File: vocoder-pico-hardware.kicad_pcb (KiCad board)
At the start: 2 copper layers, 47 x 108 mm, 68 parts, among them J1 Conn_02x05_Odd_Even, J2 AudioJack2_SwitchT, J3 AudioJack2_SwitchT, Q1 BC547, Q2 BC547, Q3 BC547, Q4 BC547, SW1 SW_Push, SW2 SW_Push, U1 TL072, U2 LM7805_TO220, U3 PCM5100A, U4 SC39-11GWA, U5 SC39-11GWA, U6 SC39-11GWA, U7 SC39-11GWA, U8 MCP6002-xP

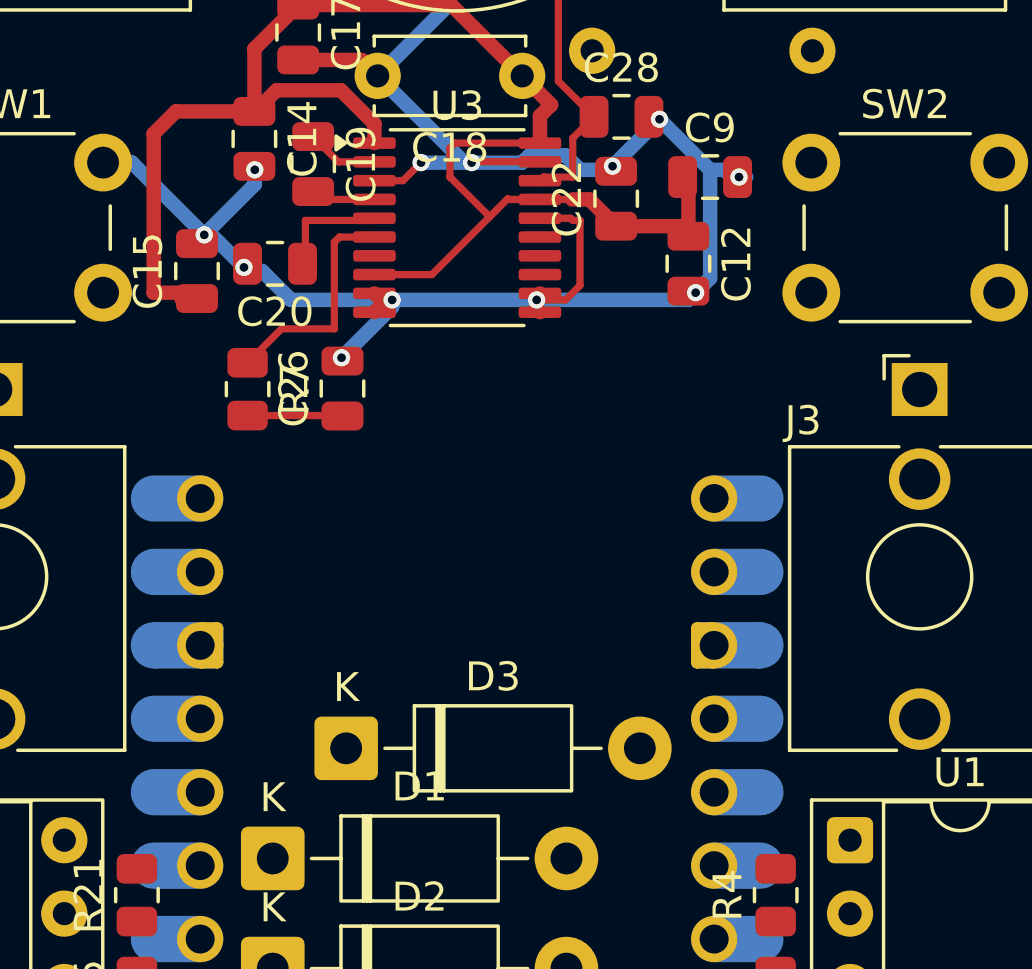
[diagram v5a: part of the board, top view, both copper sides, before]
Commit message: begin routing of i2s section
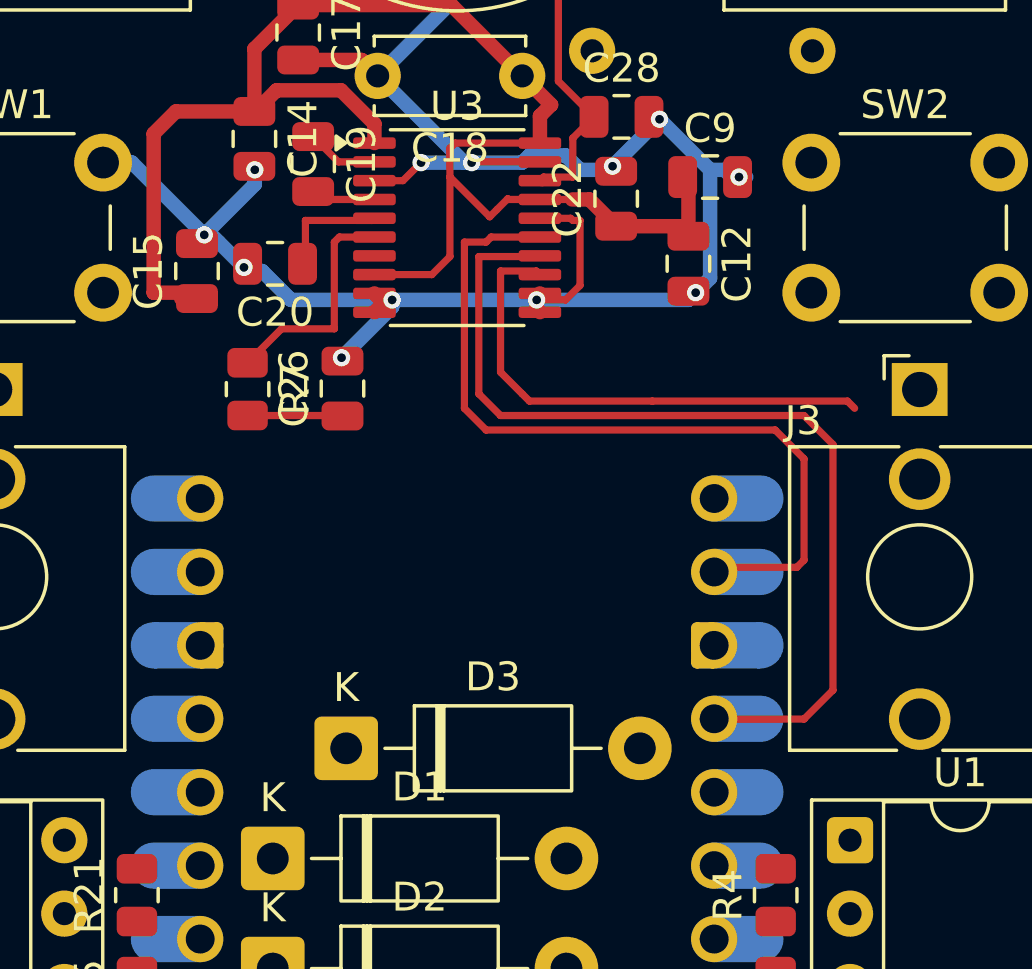
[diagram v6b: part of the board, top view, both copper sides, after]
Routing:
- net Net-(A1-GPIO18): track 0.00 -> 32.9 mm
- net Net-(A1-GPIO17): track 0.00 -> 27.7 mm
- net Net-(A1-GPIO16): track 0.00 -> 17.7 mm
- net Vdd: track 54.3 -> 55.1 mm
- net Net-(A1-GPIO12): track 0.00 -> 0.80 mm
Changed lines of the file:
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@@
+	)
+	(segment
+		(start 84.25 84)
+		(end 91 84)
+		(width 0.25)
+		(layer "F.Cu")
+		(net 9)
+	)
+	(segment
+		(start 79 83)
+		(end 79.75 83.75)
+		(width 0.25)
+		(layer "F.Cu")
+		(net 9)
+	)
+	(segment
+		(start 80.2375 79.5)
+		(end 79 79.5)
+		(width 0.25)
+		(layer "F.Cu")
+		(net 9)
+	)
+	(segment
+		(start 80 84)
+		(end 84.25 84)
+		(width 0.25)
+		(layer "F.Cu")
+		(net 9)
+	)
+	(segment
+		(start 79.75 83.75)
+		(end 80 84)
+		(width 0.25)
+		(layer "F.Cu")
+		(net 9)
+	)
+	(segment
+		(start 91 84)
+		(end 91.25 84.25)
+		(width 0.25)
+		(layer "F.Cu")
+		(net 9)
+	)
+	(segment
+		(start 80.3625 79.625)
+		(end 80.2375 79.5)
+		(width 0.25)
+		(layer "F.Cu")
+		(net 9)
+	)
+	(segment
+		(start 79 79.5)
+		(end 79 83)
+		(width 0.25)
+		(layer "F.Cu")
+		(net 9)
 	)
 	(segment
@@
 	)
 	(segment
+		(start 77.25 79)
+		(end 77.25 76.25)
+		(width 0.25)
+		(layer "F.Cu")
+		(net 20)
+	)
+	(segment
 		(start 77.425 75.075)
 		(end 77.25 75.25)
@@
 	(segment
 		(start 76.625 79.625)
-		(end 78.625 77.625)
+		(end 77.25 79)
 		(width 0.25)
 		(layer "F.Cu")
@@
 	)
 	(segment
+		(start 86.55 89.75)
+		(end 86.39 89.91)
+		(width 0.25)
+		(layer "F.Cu")
+		(net 25)
+	)
+	(segment
+		(start 80.3625 78.325)
+		(end 78.675 78.325)
+		(width 0.25)
+		(layer "F.Cu")
+		(net 25)
+	)
+	(segment
+		(start 89.5 89.5)
+		(end 89.25 89.75)
+		(width 0.25)
+		(layer "F.Cu")
+		(net 25)
+	)
+	(segment
+		(start 78.675 78.325)
+		(end 78.5 78.5)
+		(width 0.25)
+		(layer "F.Cu")
+		(net 25)
+	)
+	(segment
+		(start 89.5 86)
+		(end 89.5 89.5)
+		(width 0.25)
+		(layer "F.Cu")
+		(net 25)
+	)
+	(segment
+		(start 88.5 85)
+		(end 89.5 86)
+		(width 0.25)
+		(layer "F.Cu")
+		(net 25)
+	)
+	(segment
+		(start 77.75 78.5)
+		(end 77.75 84.25)
+		(width 0.25)
+		(layer "F.Cu")
+		(net 25)
+	)
+	(segment
+		(start 89.25 89.75)
+		(end 86.55 89.75)
+		(width 0.25)
+		(layer "F.Cu")
+		(net 25)
+	)
+	(segment
+		(start 77.75 84.25)
+		(end 78.5 85)
+		(width 0.25)
+		(layer "F.Cu")
+		(net 25)
+	)
+	(segment
+		(start 78.5 78.5)
+		(end 77.75 78.5)
+		(width 0.25)
+		(layer "F.Cu")
+		(net 25)
+	)
+	(segment
+		(start 78.5 85)
+		(end 88.5 85)
+		(width 0.25)
+		(layer "F.Cu")
+		(net 25)
+	)
+	(segment
+		(start 79 84.5)
+		(end 89.5 84.5)
+		(width 0.25)
+		(layer "F.Cu")
+		(net 28)
+	)
+	(segment
+		(start 86.4 95)
+		(end 86.39 94.99)
+		(width 0.25)
+		(layer "F.Cu")
+		(net 28)
+	)
+	(segment
+		(start 78.25 83.75)
+		(end 79 84.5)
+		(width 0.25)
+		(layer "F.Cu")
+		(net 28)
+	)
+	(segment
+		(start 90.5 94)
+		(end 89.5 95)
+		(width 0.25)
+		(layer "F.Cu")
+		(net 28)
+	)
+	(segment
+		(start 78.25 79)
+		(end 78.25 83.75)
+		(width 0.25)
+		(layer "F.Cu")
+		(net 28)
+	)
+	(segment
+		(start 80.3375 79)
+		(end 78.25 79)
+		(width 0.25)
+		(layer "F.Cu")
+		(net 28)
+	)
+	(segment
+		(start 80.3625 78.975)
+		(end 80.3375 79)
+		(width 0.25)
+		(layer "F.Cu")
+		(net 28)
+	)
+	(segment
+		(start 90.5 85.5)
+		(end 90.5 94)
+		(width 0.25)
+		(layer "F.Cu")
+		(net 28)
+	)
+	(segment
+		(start 89.5 84.5)
+		(end 90.5 85.5)
+		(width 0.25)
+		(layer "F.Cu")
+		(net 28)
+	)
+	(segment
+		(start 89.5 95)
+		(end 86.4 95)
+		(width 0.25)
+		(layer "F.Cu")
+		(net 28)
+	)
+	(segment
+		(start 67.81 97.53)
+		(end 68.61 97.53)
+		(width 0.25)
+		(layer "B.Cu")
+		(net 34)
+	)
+	(segment

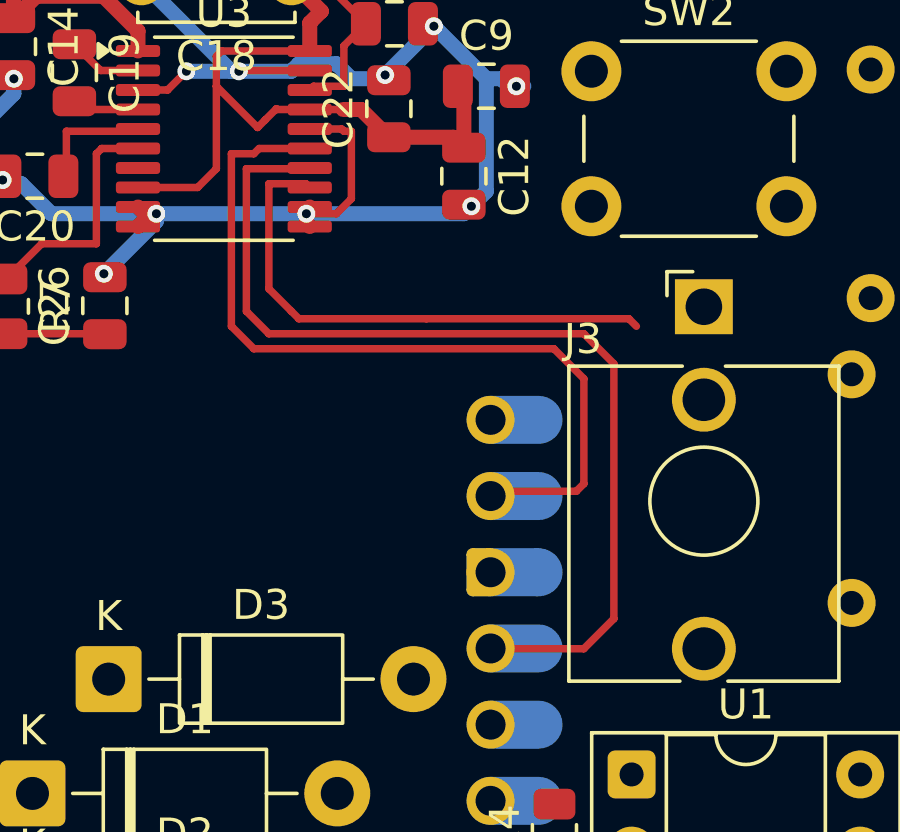
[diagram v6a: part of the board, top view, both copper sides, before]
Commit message: finish routing of i2s section
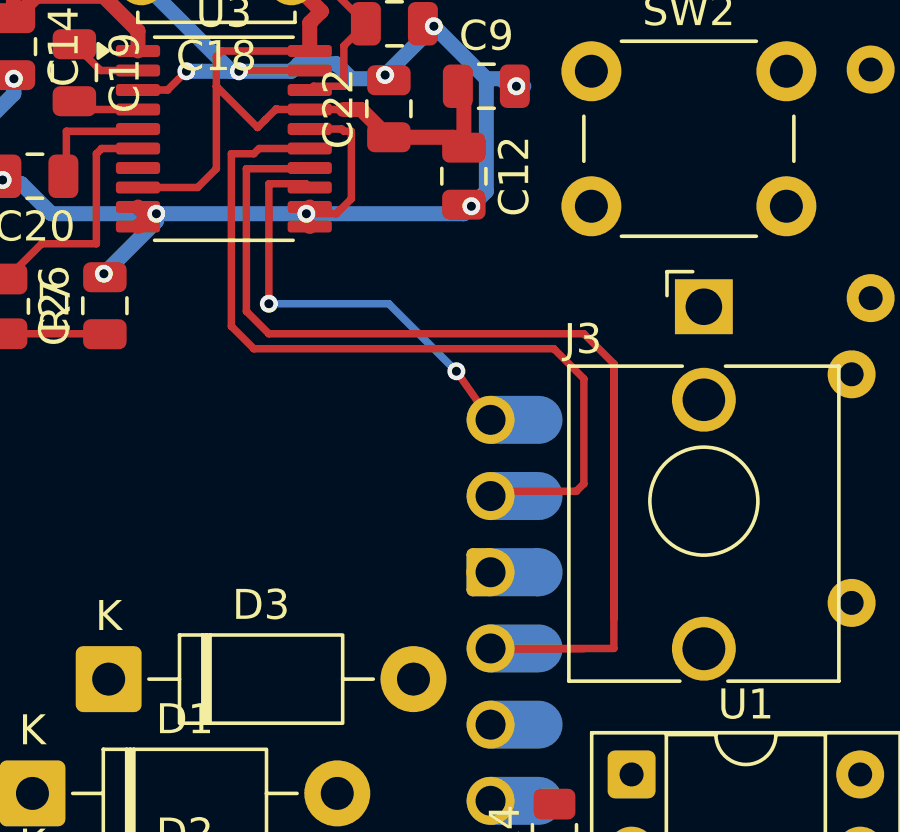
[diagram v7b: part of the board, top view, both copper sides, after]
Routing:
- net Net-(A1-GPIO18): track 32.9 -> 45.1 mm
- net Net-(A1-GPIO16): track 17.7 -> 14.6 mm, vias 0 -> 2
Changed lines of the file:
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@@
 		)
 		(group ""
-			(members "009f8124-1b45-4e31-9438-cc4fed704d9d" "03ee111c-feea-4774-a166-34cc33a90046"
-				"04b5d92a-973a-4e2c-9de7-c4f892ccba09" "0edea316-a469-4f48-99cc-f5e2aa899aa5"
-				"10275268-ab16-4f8d-94ab-af11b3473030" "10677d20-2c65-483b-971c-0e00e9308ac9"
-				"12d1a907-2073-414e-b091-82bf3433eeb4" "139e8c07-a5a8-42de-821a-48663f8872dc"
-				"22e40a83-25e2-4512-93f2-3920795f1a02" "27900012-6474-4733-bab7-587d6b919043"
-				"284d98ff-d42d-4e62-925b-06cfff97cace" "346bda35-f41c-4cbf-88c4-2abba216f60a"
-				"3cc6327f-1a53-4320-a712-275bc480aa57" "3f6408a2-26f8-4559-8606-ea183752b832"
-				"41e924ad-95f1-4019-b658-e89f23445bfe" "4b15996f-2b1a-449e-9218-f7f6b60cdc9c"
-				"5412545a-8adc-467e-ae2e-71fdfa603f02" "57d2637e-7184-40d2-a078-906976be435d"
-				"5c79790c-4421-47d2-85f5-8322e1193605" "5ff3ab04-32cd-4403-9c29-1a1c322c2d71"
-				"66212d3a-bb69-4b4b-a1ac-fe589a199646" "67033152-2a73-4422-9f4c-2768253b2ada"
-				"6cc87798-60f7-4ab4-8108-ca0061977708" "7265f749-9763-44ac-a093-4b6b8f5a6a8f"
-				"7318e646-9334-49a2-a743-cba84f0d616a" "7b9b2aa6-26aa-45c8-98bd-03da3004916f"
-				"7cb21203-1216-43ff-b47e-f31dad75a76b" "7f09ef4f-d352-4e96-841a-4178b46d1244"
-				"8ca546b0-7a9c-4aef-b730-63ecf2fa2187" "8d4d9c62-99c9-4ecf-9263-82dadf3be469"
-				"8f6f793d-6449-44f1-99a8-c8f0a246cd92" "903c5ac8-dcac-4e8f-b600-9dbe96789349"
-				"9ec248ec-926b-4cdb-b6f7-c41417b98019" "a69641de-b456-456e-9785-1ccfceac7280"
-				"aaaa7558-90ea-4597-bccc-7306acf96c19" "c0ac7c66-e9aa-414b-824f-79f36fac6145"
-				"c3a82017-bd09-4272-8b2b-6921964b577d" "cb48767a-b988-4ed7-b186-6a76fb97eec9"
-				"d3d96aac-00f6-4de3-a0ee-1c7e229e9131" "dfafd28f-12e3-431b-8d6b-fc6b58c895c2"
-				"e3e2d502-d098-4027-a75e-9bdc6413e466" "e4db54f0-7936-41bb-aac8-a2dbe82f2e13"
-				"e515b6fa-2285-448e-af32-21c32724a07d" "e60c51d1-61da-41b8-a0e9-2c5e82c12bbe"
-				"eecc856c-2508-4db3-b5f9-e69a6f88b756" "f80c8f36-08ba-410a-867c-9e97177c97f6"
-				"fac6cdb0-a7ae-4019-86e0-a896c4eb5ef8" "fe716b57-6181-4244-a338-4c4c65199e1e"
-			)
-		)
-		(group ""
-			(members "183bb400-6a1e-44b1-b4a3-b6c486547115" "1c606f4d-8881-41f4-a538-ed187908433d"
-				"1f725ecc-7009-4a4a-a034-cb07b5496723" "2899fd63-42e4-40f0-9a11-e24a8fddb3f9"
-				"3918764f-9886-4db8-ae04-826e4405f0f9" "4317d807-2dd6-48a0-8c34-937a53805c7a"
-				"43f318f2-d4d1-4f68-bea5-dd9fbbb524d0" "4544cf40-75b4-4af5-8a3f-dc58ea5c786c"
-				"46145a36-c7ab-4879-9ca7-1b4c683e469a" "54490043-ca01-4787-b874-9861627f05db"
-				"7baeda15-288b-4625-abd4-23171e82f59a" "8101aca1-a037-4e11-92b3-765593099ff8"
-				"83d68f9f-e4a4-485f-89d2-7e1937845d2d" "8b4cbe61-49c7-45c7-b1fb-e64255d738b6"
-				"91b94f4d-4e12-4a3c-b3b7-61c8731bef7b" "9e8a3714-714e-400b-af12-f56dae0b7234"
-				"af0384a5-fafe-4eca-aebf-6f6d00789b46" "d214f8de-ea44-4439-a46e-389771060a2d"
-				"f8ff8a6f-6340-4ccf-b3bc-2fe974921e15" "fd3ea537-e78d-4872-9a26-dba08ea7192f"
-			)
-		)
-		(group ""
-			(members "015ae03d-ee05-4f9b-a215-e1abc6528629" "017bf0f2-3da3-459d-849d-940f8b4c6e4b"
-				"11d3d397-7315-47f2-a934-7ea52281d7eb" "1c12e14a-2df5-4dbf-a6a4-afba3d1bea48"
-				"2c62fe67-55f5-4f82-9a63-d7dd18ff830a" "3a829db5-5a9f-4418-8790-26e01c9fdd85"
-				"404a968b-57b9-4ae7-a338-2f38ef4e22c3" "4fa41438-cfbd-405b-9c45-268387e7137e"
-				"5e0776ae-d4ad-40e2-8bb7-ad00d7dbb088" "66a287d6-f63d-4e00-9257-a757968b320e"
-				"6e93798b-f522-411f-9015-4b399a424e9a" "75a6dfec-08b4-4708-9c98-e9254661d925"
-				"846106cf-aa95-4c9a-9865-d9e615c56c11" "907074bd-5251-4362-a718-67944e0b45f3"
-				"a68ee05b-e8d6-4447-9a74-692ba455c012" "a7ba8daf-e5b2-4239-ad93-24fe48200e58"
-				"ab45c821-c18f-4d79-bd24-b46bea0b5972" "b14d7d99-ae10-4982-b4d1-f34175ce8ad2"
-				"b162f566-0a10-4e9d-9c8c-8d0f25aeef53" "b32916cf-f0cc-44c2-a0f7-2919b13669c1"
-				"b8c6d914-bf86-4951-9442-84e237a47894" "ce8c8d5e-154f-4cd6-8300-463f8daddbc4"
-				"ced6a322-bf42-4314-9f5c-ca7c5eaf4117" "d1225fe6-4afe-4172-96da-2736cd2f9ca8"
-				"d3bea332-f0e1-435f-9d42-c569b416069c" "d977acdb-fc67-4dd9-bb28-9adf106be36d"
-				"dd4d3ab8-d4e9-434b-b3f0-98d06da793fc" "e05794f7-a1b0-4bf4-b5e0-3dd511a38505"
-			)
-		)
-		(group ""
 			(members "009f8124-1b45-4e31-9438-cc4fed704d9d" "01f7b3f9-6ebd-466e-9a2d-50a302f197de"
 				"03ee111c-feea-4774-a166-34cc33a90046" "04b5d92a-973a-4e2c-9de7-c4f892ccba09"
@@
 		)
 		(group ""
+			(members "183bb400-6a1e-44b1-b4a3-b6c486547115" "1c606f4d-8881-41f4-a538-ed187908433d"
+				"1f725ecc-7009-4a4a-a034-cb07b5496723" "2899fd63-42e4-40f0-9a11-e24a8fddb3f9"
+				"3918764f-9886-4db8-ae04-826e4405f0f9" "4317d807-2dd6-48a0-8c34-937a53805c7a"
+				"43f318f2-d4d1-4f68-bea5-dd9fbbb524d0" "4544cf40-75b4-4af5-8a3f-dc58ea5c786c"
+				"46145a36-c7ab-4879-9ca7-1b4c683e469a" "54490043-ca01-4787-b874-9861627f05db"
+				"7baeda15-288b-4625-abd4-23171e82f59a" "8101aca1-a037-4e11-92b3-765593099ff8"
+				"83d68f9f-e4a4-485f-89d2-7e1937845d2d" "8b4cbe61-49c7-45c7-b1fb-e64255d738b6"
+				"91b94f4d-4e12-4a3c-b3b7-61c8731bef7b" "9e8a3714-714e-400b-af12-f56dae0b7234"
+				"af0384a5-fafe-4eca-aebf-6f6d00789b46" "d214f8de-ea44-4439-a46e-389771060a2d"
+				"f8ff8a6f-6340-4ccf-b3bc-2fe974921e15" "fd3ea537-e78d-4872-9a26-dba08ea7192f"
+			)
+		)
+		(group ""
+			(members "015ae03d-ee05-4f9b-a215-e1abc6528629" "017bf0f2-3da3-459d-849d-940f8b4c6e4b"
+				"11d3d397-7315-47f2-a934-7ea52281d7eb" "1c12e14a-2df5-4dbf-a6a4-afba3d1bea48"
+				"2c62fe67-55f5-4f82-9a63-d7dd18ff830a" "3a829db5-5a9f-4418-8790-26e01c9fdd85"
+				"404a968b-57b9-4ae7-a338-2f38ef4e22c3" "4fa41438-cfbd-405b-9c45-268387e7137e"
+				"5e0776ae-d4ad-40e2-8bb7-ad00d7dbb088" "66a287d6-f63d-4e00-9257-a757968b320e"
+				"6e93798b-f522-411f-9015-4b399a424e9a" "75a6dfec-08b4-4708-9c98-e9254661d925"
+				"846106cf-aa95-4c9a-9865-d9e615c56c11" "907074bd-5251-4362-a718-67944e0b45f3"
+				"a68ee05b-e8d6-4447-9a74-692ba455c012" "a7ba8daf-e5b2-4239-ad93-24fe48200e58"
+				"ab45c821-c18f-4d79-bd24-b46bea0b5972" "b14d7d99-ae10-4982-b4d1-f34175ce8ad2"
+				"b162f566-0a10-4e9d-9c8c-8d0f25aeef53" "b32916cf-f0cc-44c2-a0f7-2919b13669c1"
+				"b8c6d914-bf86-4951-9442-84e237a47894" "ce8c8d5e-154f-4cd6-8300-463f8daddbc4"
+				"ced6a322-bf42-4314-9f5c-ca7c5eaf4117" "d1225fe6-4afe-4172-96da-2736cd2f9ca8"
+				"d3bea332-f0e1-435f-9d42-c569b416069c" "d977acdb-fc67-4dd9-bb28-9adf106be36d"
+				"dd4d3ab8-d4e9-434b-b3f0-98d06da793fc" "e05794f7-a1b0-4bf4-b5e0-3dd511a38505"
+			)
+		)
+		(group ""
 			(members "91f61ad2-4691-4903-82cb-bc7c4aff599e" "a56f600f-cff4-4fa9-9926-d6abf895d0c9")
 		)
 		(group ""
+			(members "10275268-ab16-4f8d-94ab-af11b3473030" "22e40a83-25e2-4512-93f2-3920795f1a02"
+				"27900012-6474-4733-bab7-587d6b919043" "57d2637e-7184-40d2-a078-906976be435d"
+				"67033152-2a73-4422-9f4c-2768253b2ada" "8f6f793d-6449-44f1-99a8-c8f0a246cd92"
+				"d3d96aac-00f6-4de3-a0ee-1c7e229e9131" "e515b6fa-2285-448e-af32-21c32724a07d"
+			)
+		)
+		(group ""
 			(members "02dd6f8a-cab1-4391-aea0-039ce353b80d" "05afa30a-c2f1-47a2-b5a9-6f9e603712d7"
 				"10464f26-9c76-4013-b0fc-43de6dd5a3c5" "25bad425-c59d-4396-b392-4f0463a8465c"
@@
 	)
 	(segment
-		(start 84.25 84)
-		(end 91 84)
+		(start 85.25 85.75)
+		(end 86.39 87.37)
 		(width 0.25)
 		(layer "F.Cu")
@@
 	)
 	(segment
-		(start 79 83)
-		(end 79.75 83.75)
+		(start 79 79.5)
+		(end 79 83.5)
 		(width 0.25)
 		(layer "F.Cu")
@@
 	)
 	(segment
-		(start 80 84)
-		(end 84.25 84)
+		(start 80.3625 79.625)
+		(end 80.2375 79.5)
 		(width 0.25)
 		(layer "F.Cu")
 		(net 9)
 	)
-	(segment
-		(start 79.75 83.75)
-		(end 80 84)
-		(width 0.25)
-		(layer "F.Cu")
+	(via
+		(at 85.25 85.75)
+		(size 0.6)
+		(drill 0.3)
+		(layers "F.Cu" "B.Cu")
 		(net 9)
 	)
-	(segment
-		(start 91 84)
-		(end 91.25 84.25)
-		(width 0.25)
-		(layer "F.Cu")
+	(via
+		(at 79 83.5)
+		(size 0.6)
+		(drill 0.3)
+		(layers "F.Cu" "B.Cu")
 		(net 9)
 	)
 	(segment
-		(start 80.3625 79.625)
-		(end 80.2375 79.5)
+		(start 79 83.5)
+		(end 83 83.5)
 		(width 0.25)
-		(layer "F.Cu")
+		(layer "B.Cu")
 		(net 9)
 	)
 	(segment
-		(start 79 79.5)
-		(end 79 83)
+		(start 83 83.5)
+		(end 85.25 85.75)
 		(width 0.25)
-		(layer "F.Cu")
+		(layer "B.Cu")
 		(net 9)
 	)
@@
 	)
 	(segment
-		(start 90.5 94)
-		(end 89.5 95)
+		(start 90.5 94.99)
+		(end 86.39 94.99)
+		(width 0.25)
+		(layer "F.Cu")
+		(net 28)
+	)
+	(segment
+		(start 90.5 85.5)
+		(end 90.5 94.99)
 		(width 0.25)
 		(layer "F.Cu")
